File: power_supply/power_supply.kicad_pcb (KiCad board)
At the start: 2 copper layers, 50 parts, among them J1 Conn_01x04_Male, J2 Conn_01x03_Male, J3 Conn_01x03_Male, J4 Conn_01x03_Male, J5 Conn_01x02_Male, U1 LM7815_TO220, U2 LM7915_TO220, U3 LM7815_TO220

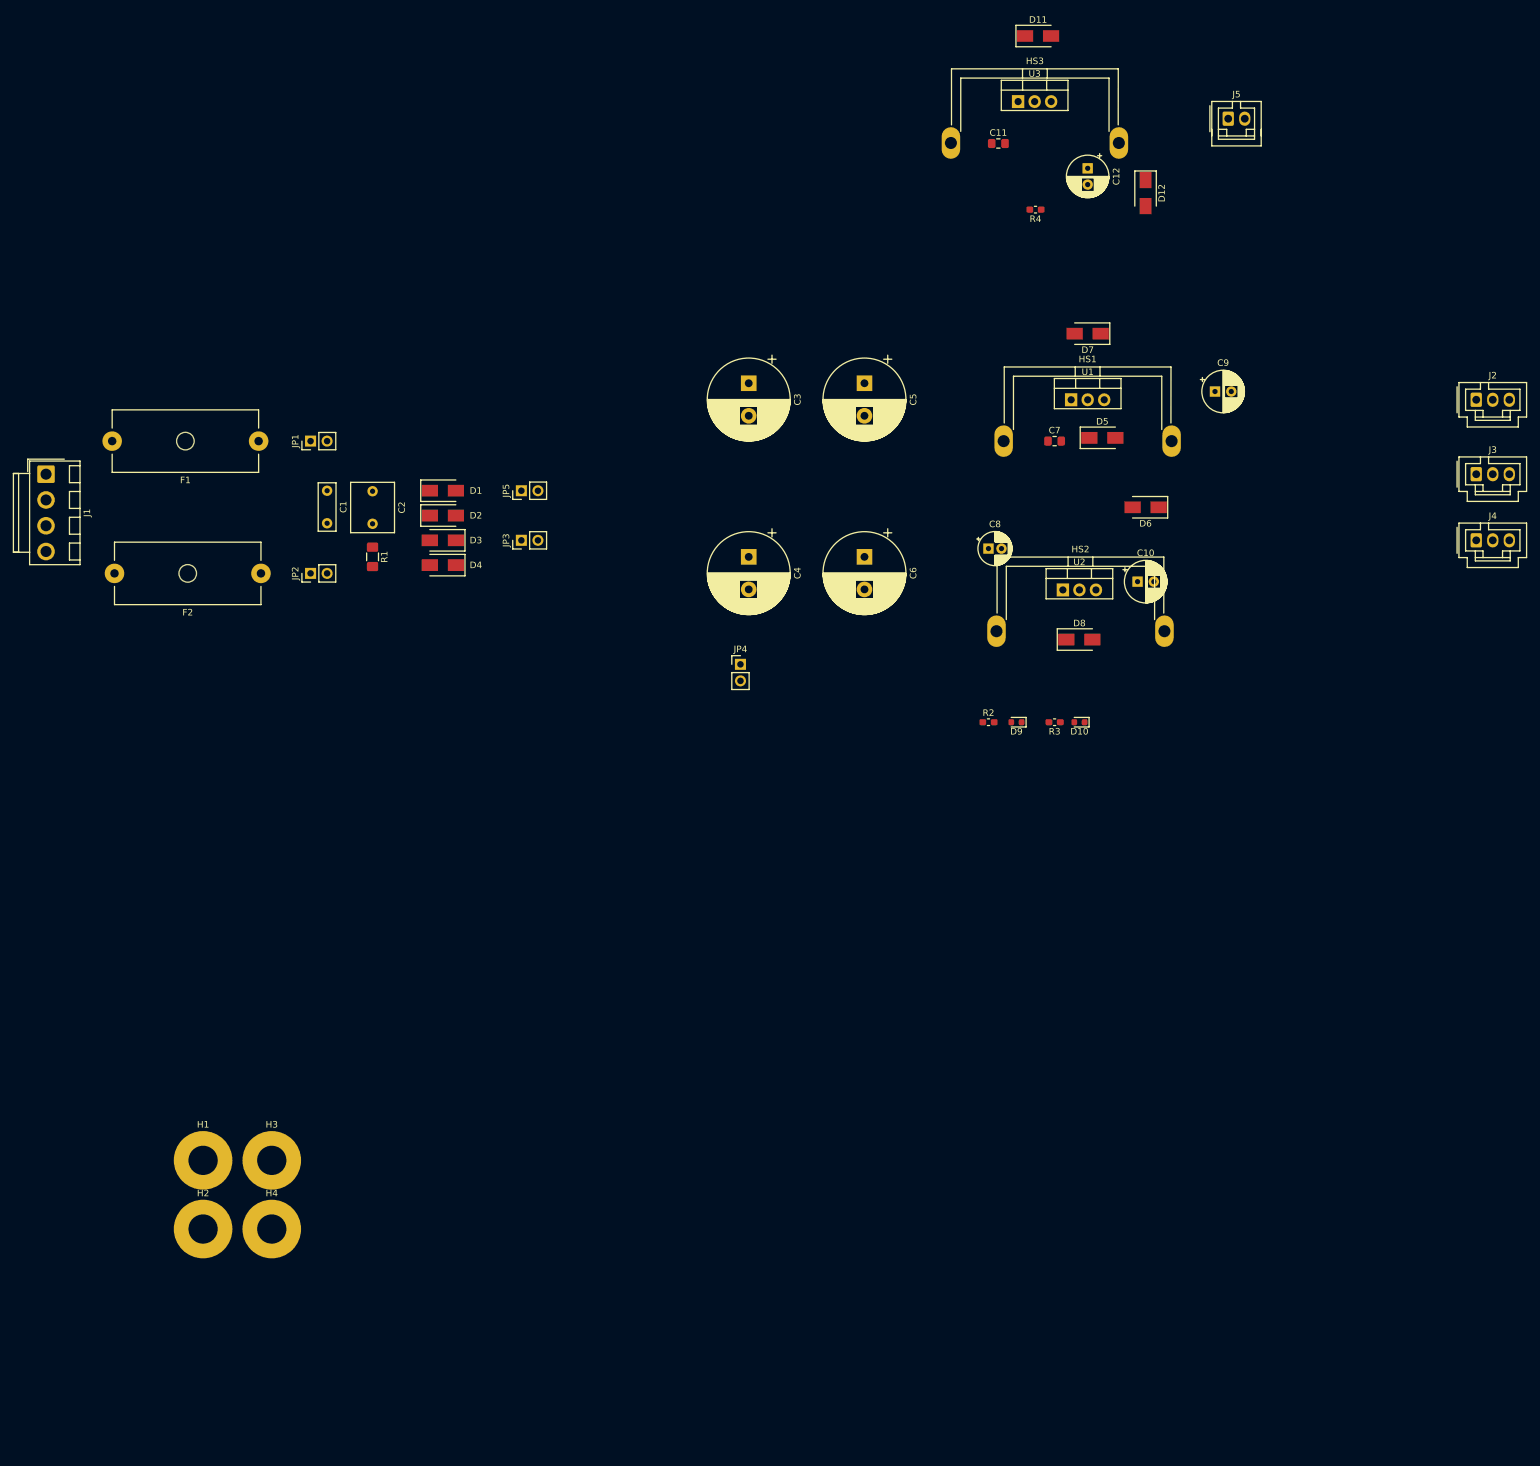
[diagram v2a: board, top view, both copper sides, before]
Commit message: complete most initial layout
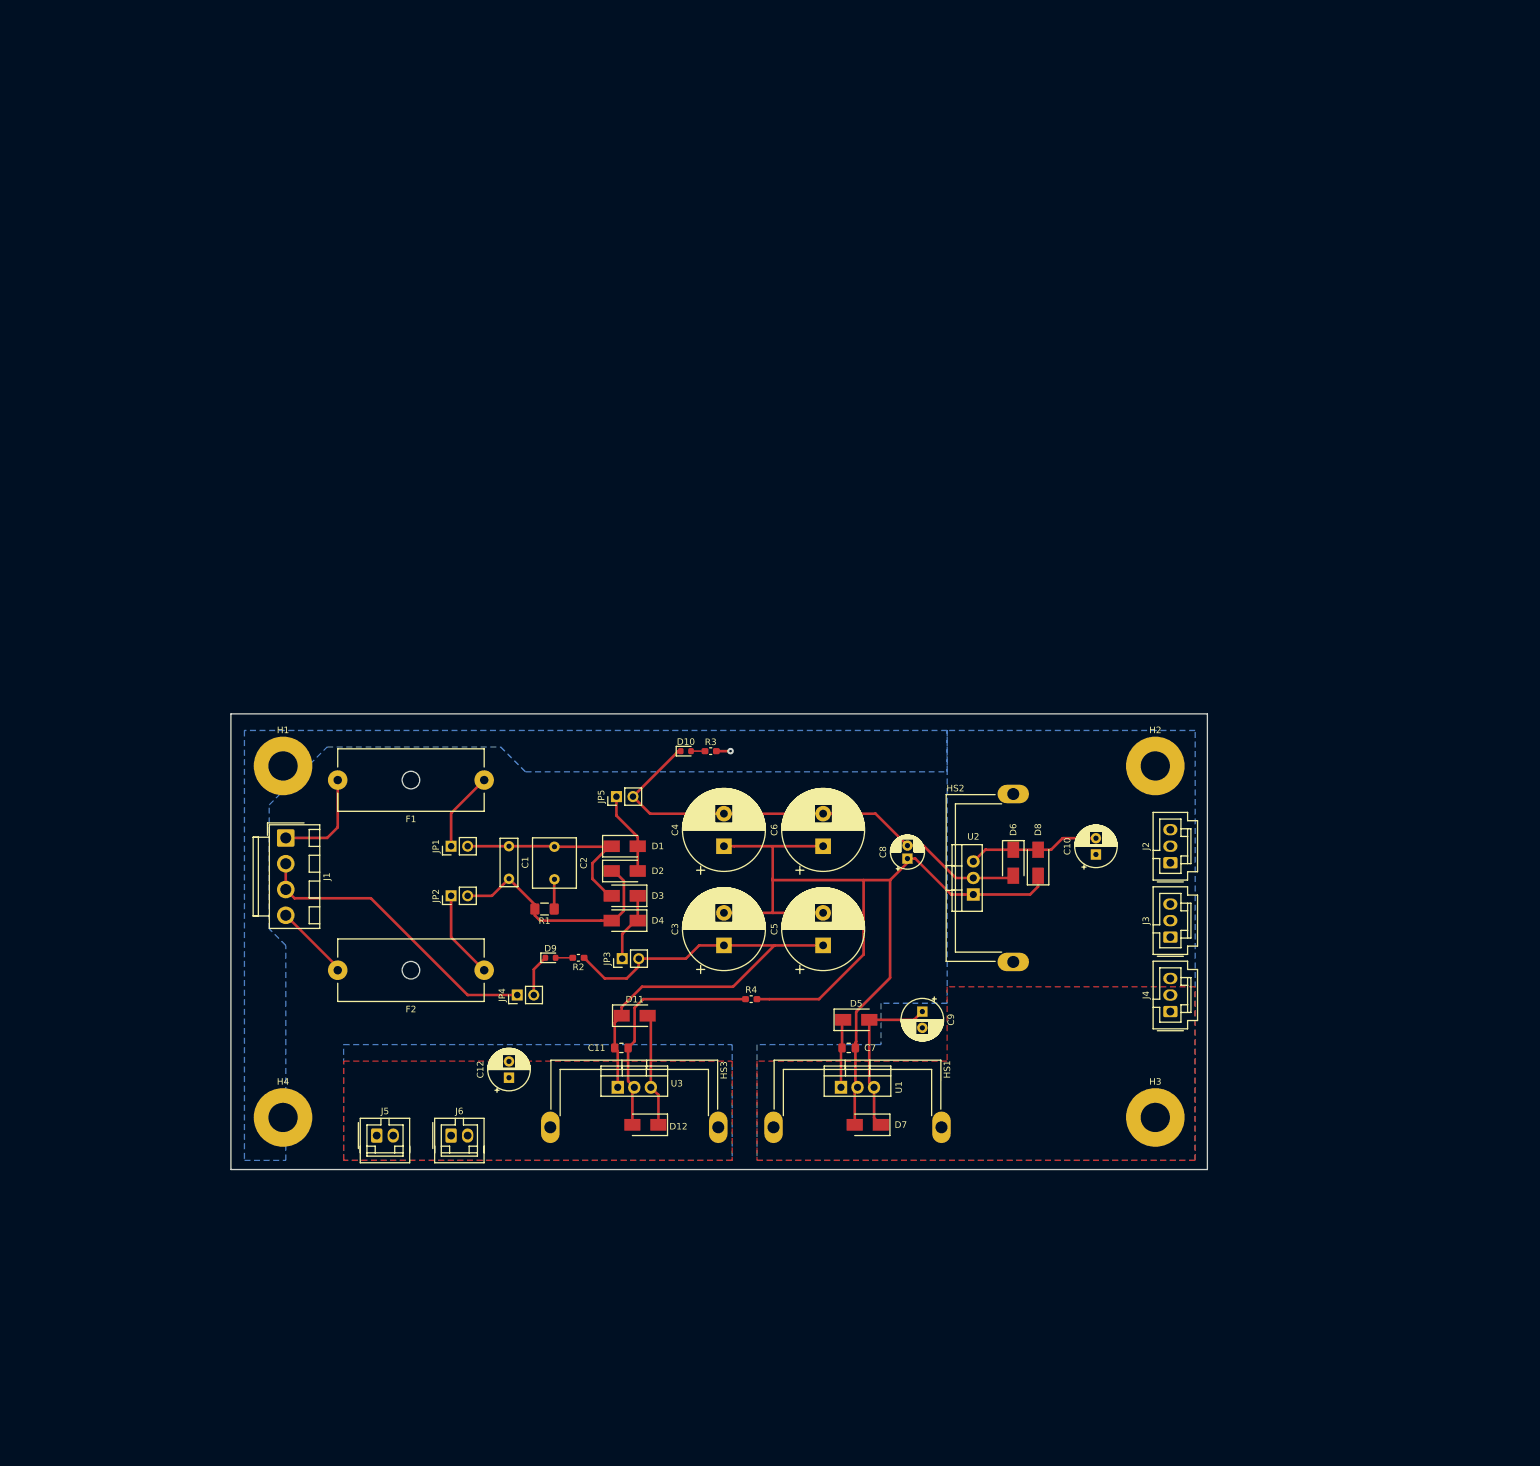
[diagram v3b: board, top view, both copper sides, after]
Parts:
- added J6: Conn_01x02_Male, Connector_Molex_SL:Molex_SL_A-70543-0001_1x02_P2.54mm_Vertical, F.Cu at (83.8, 144.8)
- HS1, HS2, HS3: value Heatsink_Pad -> Wakefield-Vette 287-1AB
- moved J5 203.7 mm to (72.4, 144.8)
- moved C12 165.6 mm to (92.7, 135.9), turned to 90 degrees
- moved U3 163.4 mm to (109.4, 137.4)
- moved HS3 163.3 mm to (99.1, 143.5)
- moved D11 162.8 mm to (112.0, 126.4)
- moved H2 162.7 mm to (192.0, 88.0)
- moved D12 162.4 mm to (113.7, 143.1), turned to 180 degrees
- moved C11 150.5 mm to (110.0, 131.3)
- moved H3 135.9 mm to (192.0, 142.0)
- moved R4 128.9 mm to (129.9, 123.8), turned to 0 degrees
- moved D7 126.1 mm to (147.8, 143.1)
- moved U1 111.4 mm to (143.7, 137.4)
- moved HS1 111.2 mm to (133.3, 143.5)
- moved C9 105.3 mm to (156.2, 125.7), turned to 270 degrees
- moved C7 98.4 mm to (144.9, 131.3)
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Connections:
- HS1 pad 1: (no net) -> GNDA
- HS2 pad 1: (no net) -> GNDA
- HS3 pad 1: (no net) -> GNDRELAY
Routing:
- net GNDA: track 0.00 -> 167.9 mm, vias 0 -> 1
- net /+15_unreg: track 0.00 -> 91.7 mm
- net /-15_unreg: track 0.00 -> 74.0 mm
- net /transformer_center: track 0.00 -> 46.2 mm
- net GNDRELAY: track 0.00 -> 36.5 mm
- net Net-(C1-Pad2): track 0.00 -> 36.4 mm
- net Net-(C1-Pad1): track 0.00 -> 32.7 mm
- net VCC: track 0.00 -> 25.6 mm
- net VEE: track 0.00 -> 20.3 mm
- net Vrelay: track 0.00 -> 17.4 mm
- net /transformer_plus: track 0.00 -> 15.9 mm
- net Net-(F2-Pad1): track 0.00 -> 13.5 mm
- net Net-(D1-Pad2): track 0.00 -> 12.8 mm
- net Net-(F1-Pad1): track 0.00 -> 12.3 mm
- net /transformer_minus: track 0.00 -> 11.7 mm
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- added copper zone on B.Cu, net GNDA
- added copper zone on B.Cu, net GNDRELAY
- added copper zone on F.Cu, net VCC
- added copper zone on F.Cu, net Vrelay
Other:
- board outline added: 150 x 70 mm
- net class grounds added: clearance 0.4, trace_width 0.4064, via_dia 1, via_drill 0.4
- net class power_reg added: clearance 0.2, trace_width 0.4064, via_dia 1, via_drill 0.4
- net class power_unreg added: clearance 0.4, trace_width 0.4064, via_dia 1, via_drill 0.4
- board text added: "TODO model for fuse model for heatsink model for input connector labels for jumpers labels for connectors labels for regulators labels for LEDs"

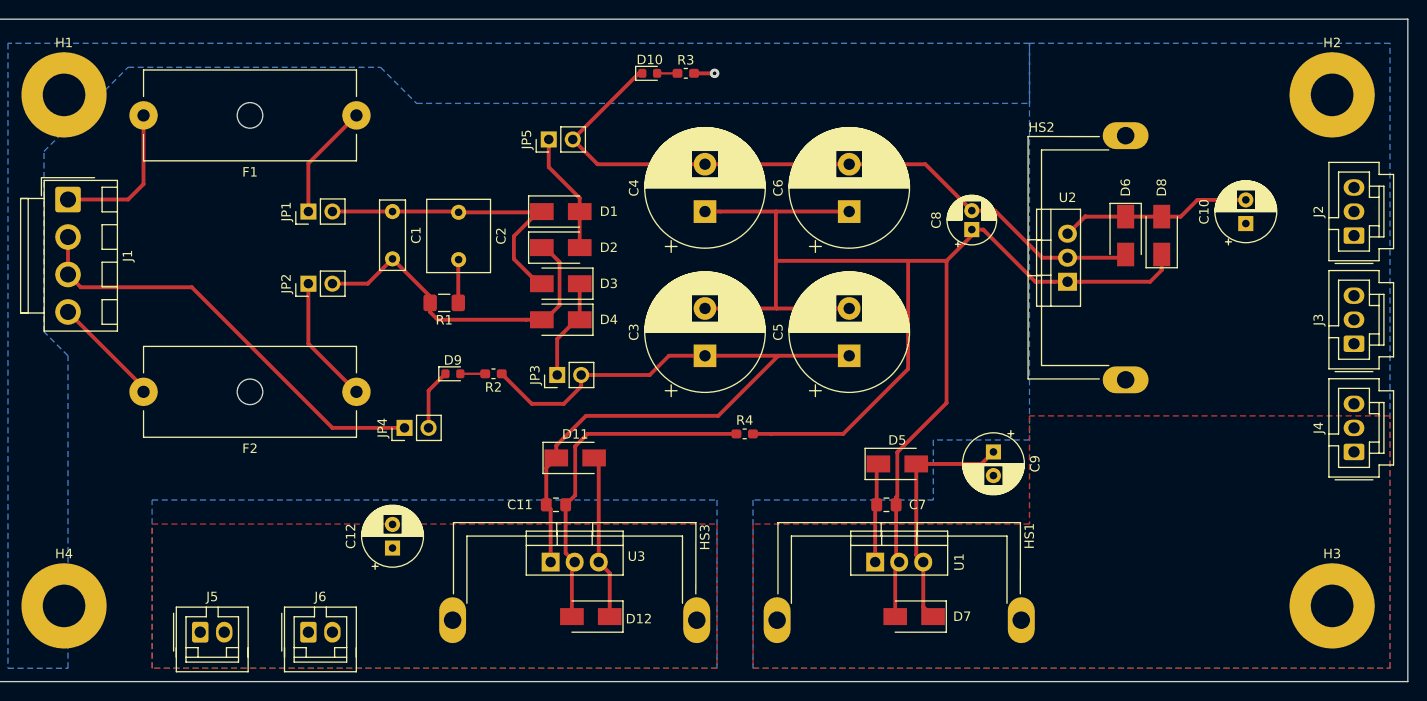
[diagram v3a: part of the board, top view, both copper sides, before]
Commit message: complete basic layout, add silkscreen labels, add all models, update TODO
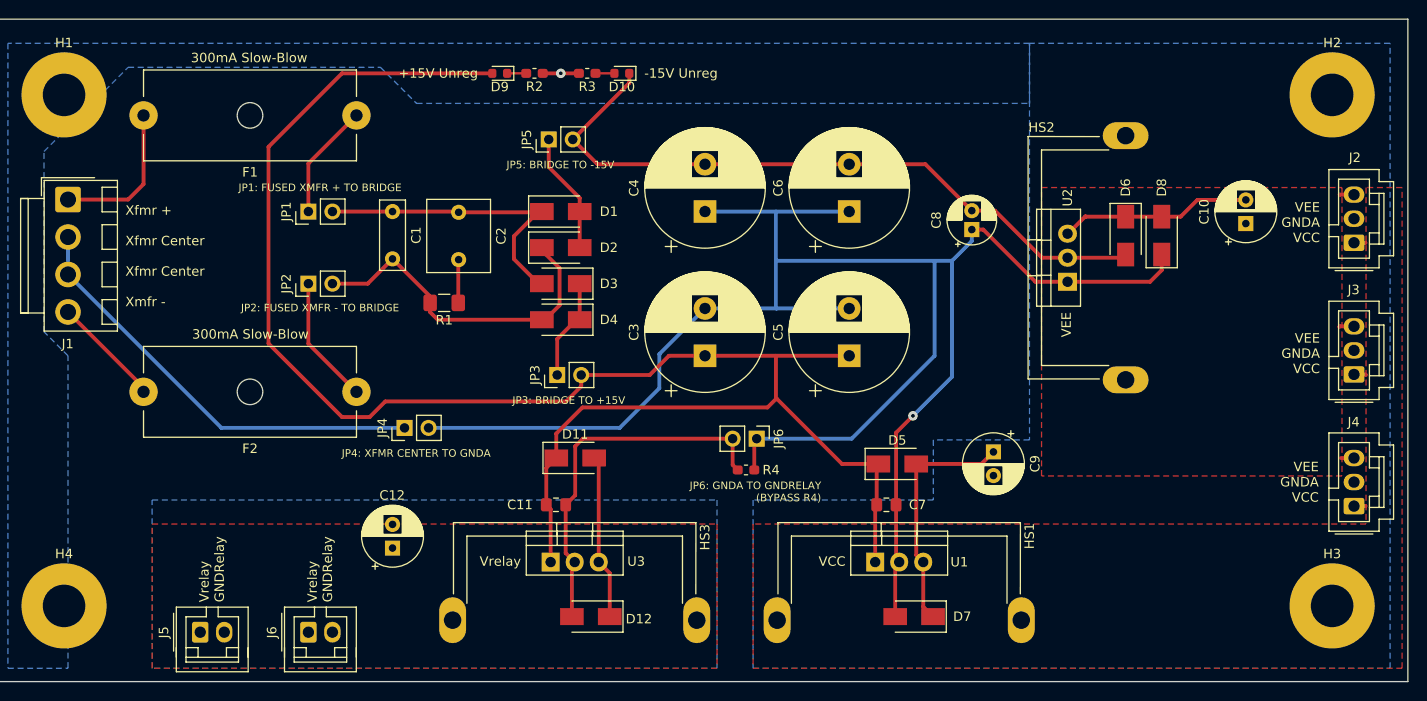
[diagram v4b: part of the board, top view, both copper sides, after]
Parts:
- added JP6: Jumper_NC_Small, Connector_PinHeader_2.54mm:PinHeader_1x02_P2.54mm_Vertical, F.Cu at (131.2, 124.3)
- moved D9 32.1 mm to (104.0, 85.7), turned to 180 degrees
- moved R2 32.0 mm to (107.7, 85.7), turned to 0 degrees
- moved R3 10.4 mm to (113.3, 85.7), turned to 0 degrees
- moved J4 5.73 mm to (194.3, 131.5)
- moved R4 3.81 mm to (130.1, 127.6)
- moved J3 3.24 mm to (194.3, 117.5)
- moved D10 2.95 mm to (116.9, 85.7), turned to 180 degrees
- moved J2 0.75 mm to (194.3, 103.6)
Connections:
- D9 pad 1: GNDA -> Net-(D9-Pad1)
- D9 pad 2: Net-(D9-Pad2) -> /+15_unreg
- R2 pad 1: /+15_unreg -> Net-(D9-Pad1)
- R2 pad 2: Net-(D9-Pad2) -> GNDA
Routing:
- net /+15_unreg: track 91.7 -> 183.6 mm
- net GNDA: track 167.9 -> 205.8 mm, vias 1 -> 2
- net VEE: track 20.3 -> 24.8 mm
- net VCC: track 25.6 -> 29.3 mm
- net GNDRELAY: track 36.5 -> 39.4 mm
- net Net-(D9-Pad2): track 2.63 -> 0.00 mm
- net Net-(D9-Pad1): track 0.00 -> 2.01 mm
- net /-15_unreg: track 74.0 -> 73.2 mm
- added copper zone on F.Cu, net VEE
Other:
- board text added: "+15V Unreg"
- board text added: "-15V Unreg"
- board text added: "300mA Slow-Blow"
- board text added: "JP1: FUSED XMFR + TO BRIDGE"
- board text added: "JP2: FUSED XMFR - TO BRIDGE"
- board text added: "JP3: BRIDGE TO +15V"
- board text added: "JP4: XFMR CENTER TO GNDA"
- board text added: "JP5: BRIDGE TO -15V"
- board text added: "JP6: GNDA TO GNDRELAY (BYPASS R4)"
- board text added: "TODO fix C9, C10 add planes make smaller"
- board text added: "VCC"
- board text added: "VEE"
- board text added: "VEE GNDA VCC"
- board text added: "Vrelay"
- board text added: "Vrelay GNDRelay"
- board text added: "Xfmr + Xfmr Center Xfmr Center Xmfr -"
- board text removed: "TODO model for fuse model for heatsink model for input connector labels for jumpers labels for connectors labels for regulators labels for LEDs"

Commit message: add symbols to board (kicad, CC, OSHW)
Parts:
- added REF**: OSHW-Logo2_9.8x8mm_SilkScreen, Symbol:OSHW-Logo2_9.8x8mm_SilkScreen, B.Cu at (181.3, 131.2)
- added REF**: Symbol_CreativeCommons_CopperTop_Type2_Small, Symbol:Symbol_CreativeCommons_CopperTop_Type2_Small, F.Cu at (207.4, 142.8)
- added REF**: Symbol_CC-ShareAlike_CopperTop_Small, Symbol:Symbol_CC-ShareAlike_CopperTop_Small, F.Cu at (220.3, 142.8)
- added REF**: Symbol_CC-Attribution_CopperTop_Small, Symbol:Symbol_CC-Attribution_CopperTop_Small, F.Cu at (214.2, 142.8)
- added REF**: KiCad-Logo2_8mm_SilkScreen, Symbol:KiCad-Logo2_8mm_SilkScreen, B.Cu at (174.8, 141.2)
